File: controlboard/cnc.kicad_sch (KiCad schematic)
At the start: 31 parts, among them J1 Conn_02x04_Counter_Clockwise, J2 Conn_02x04_Row_Letter_Last, J5 Conn_02x04_Row_Letter_First, M1 Motor_Servo, Q1 PMOS AO3401A

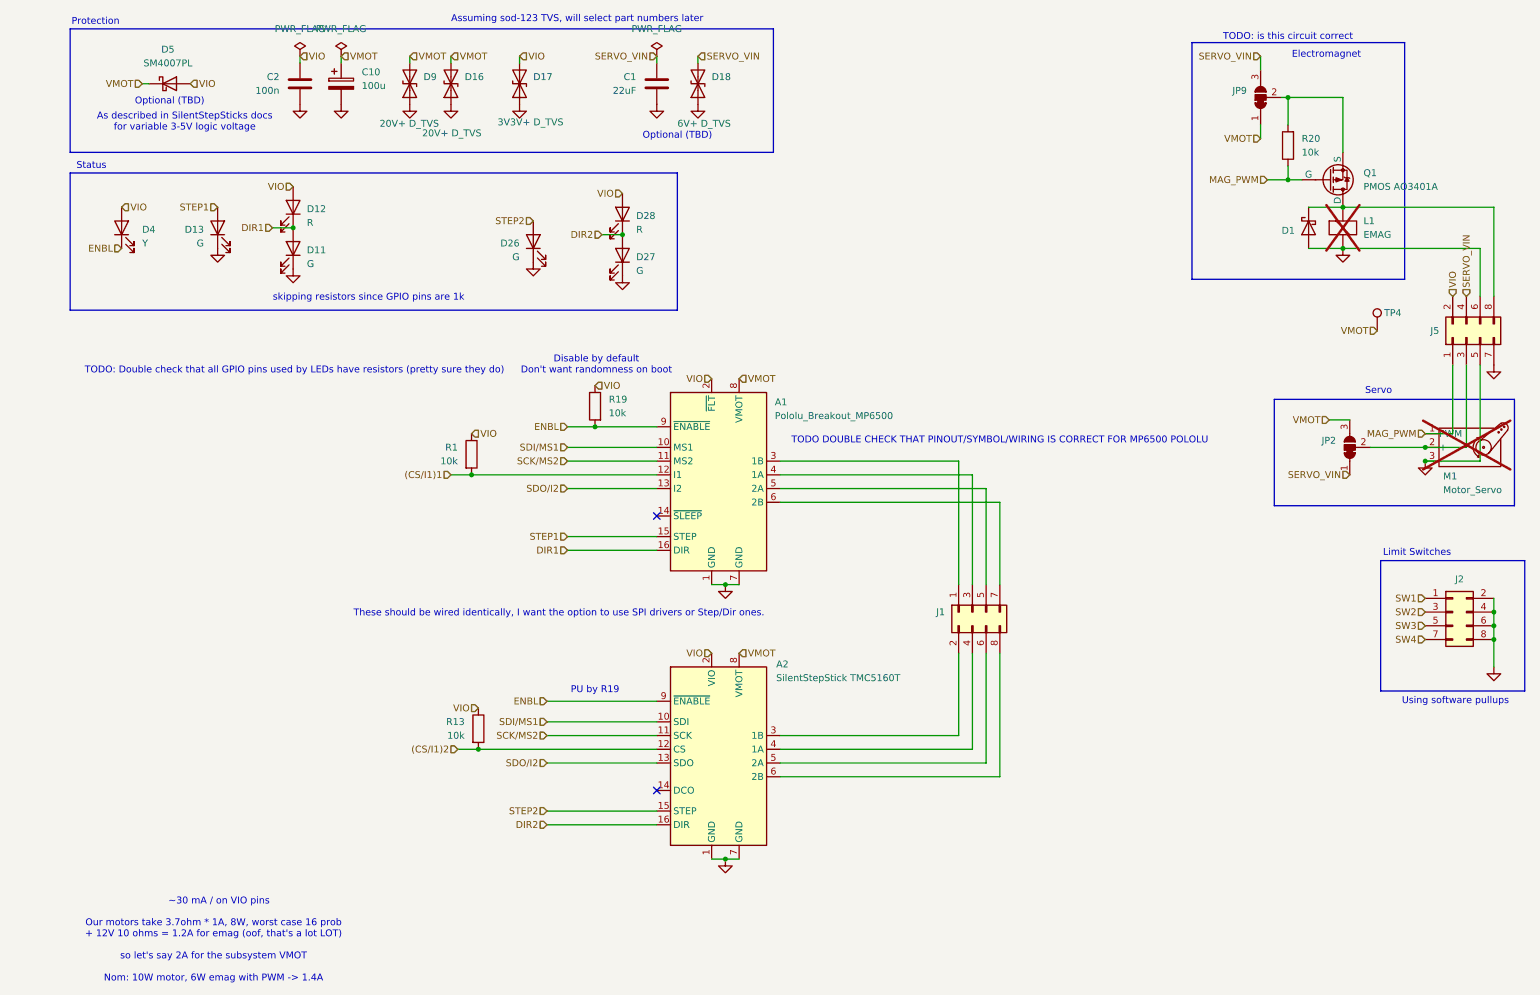
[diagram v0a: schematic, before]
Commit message: controlboard: fix critical mosfet errors
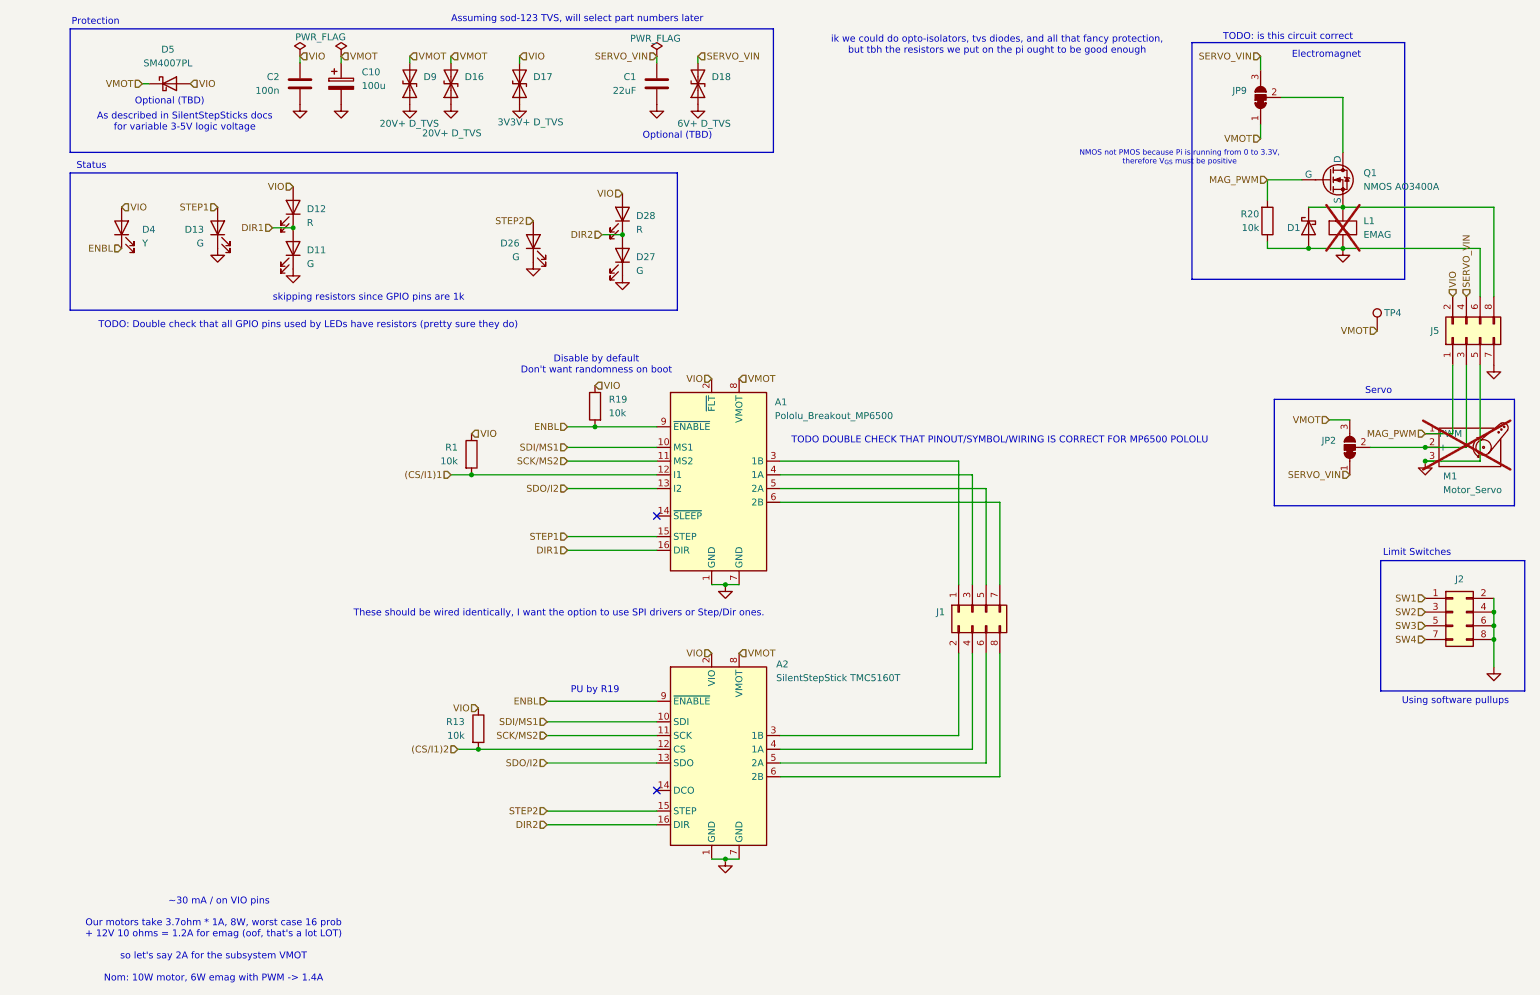
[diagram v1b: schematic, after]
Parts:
- removed Q1: PMOS AO3401A, Package_TO_SOT_SMD:SOT-23, symbol Simulation_SPICE:PMOS
- added Q1: NMOS AO3400A, Package_TO_SOT_SMD:SOT-23_Handsoldering, symbol Simulation_SPICE:NMOS
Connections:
- net GND: now also R20.1
- net MAG_PWM: now also R20.2, Q1.2 (G); no longer R20.1
- net at D1.1 (K), J5.8 (Pin_8), L1.1 (-): now also Q1.3 (S)
- net at JP9.2 (C): now also Q1.1 (D); no longer R20.2
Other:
- note added: "NMOS not PMOS because Pi is running from 0 to 3.3V, therefore V_{GS} must be positive"
- note added: "ik we could do opto-isolators, tvs diodes, and all that fancy protection, but tbh the resistors we put on the pi ought to be good enough"

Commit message: improvements
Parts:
- removed D16: 20V+ D_TVS, Diode_SMD:D_SOD-123F, symbol Device:D_TVS
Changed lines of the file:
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@@
 	(wire
 		(pts
-			(xy 83.82 22.86) (xy 83.82 24.13)
-		)
-		(stroke
-			(width 0)
-			(type default)
-		)
-	)
-	(wire
-		(pts
 			(xy 134.62 120.65) (xy 137.16 120.65)
 		)
@@
 		)
 	)
-	(hierarchical_label "VMOT"
-		(shape input)
-		(at 83.82 22.86 0)
-		(fields_autoplaced yes)
-		(effects
-			(font
-				(size 1.27 1.27)
-			)
-			(justify left)
-		)
-	)
 	(hierarchical_label "VIO"
 		(shape input)
@@
 	(symbol
 		(lib_id "Device:D_TVS")
-		(at 83.82 27.94 90)
-		(unit 1)
-		(exclude_from_sim no)
-		(in_bom yes)
-		(on_board yes)
-		(dnp no)
-		(property "Reference" "D16"
-			(at 86.36 26.6699 90)
-			(effects
-				(font
-					(size 1.27 1.27)
-				)
-				(justify right)
-			)
-		)
-		(property "Value" "20V+ D_TVS"
-			(at 78.486 37.084 90)
-			(effects
-				(font
-					(size 1.27 1.27)
-				)
-				(justify right)
-			)
-		)
-		(property "Footprint" "Diode_SMD:D_SOD-123F"
-			(at 83.82 27.94 0)
-			(effects
-				(font
-					(size 1.27 1.27)
-				)
-				(hide yes)
-			)
-		)
-		(property "Datasheet" "~"
-			(at 83.82 27.94 0)
-			(effects
-				(font
-					(size 1.27 1.27)
-				)
-				(hide yes)
-			)
-		)
-		(property "Description" "Bidirectional transient-voltage-suppression diode"
-			(at 83.82 27.94 0)
-			(effects
-				(font
-					(size 1.27 1.27)
-				)
-				(hide yes)
-			)
-		)
-		(pin "1"
-		)
-		(pin "2"
-		)
-		(instances
-			(project "controlboard"
-				(path "/2797250d-6fee-4769-b4dd-0e20ce4f0941/5be4ea58-2822-4c96-82fa-ac7323f92cc7"
-					(reference "D16")
-					(unit 1)
-				)
-			)
-		)
-	)
-	(symbol
-		(lib_id "Device:D_TVS")
 		(at 76.2 27.94 90)
 		(unit 1)
@@
 					(unit 1)
 				)
-			)
-		)
-	)
-	(symbol
-		(lib_id "power:GND")
-		(at 83.82 31.75 0)
-		(unit 1)
-		(exclude_from_sim no)
-		(in_bom yes)
-		(on_board yes)
-		(dnp no)
-		(fields_autoplaced yes)
-		(property "Reference" "#PWR010"
-			(at 83.82 38.1 0)
-			(effects
-				(font
-					(size 1.27 1.27)
-				)
-				(hide yes)
-			)
-		)
-		(property "Value" "GND"
-			(at 83.82 36.83 0)
-			(effects
-				(font
-					(size 1.27 1.27)
-				)
-				(hide yes)
-			)
-		)
-		(property "Footprint" ""
-			(at 83.82 31.75 0)
-			(effects
-				(font
-					(size 1.27 1.27)
-				)
-				(hide yes)
-			)
-		)
-		(property "Datasheet" ""
-			(at 83.82 31.75 0)
-			(effects
-				(font
-					(size 1.27 1.27)
-				)
-				(hide yes)
-			)
-		)
-		(property "Description" "Power symbol creates a global label with name \"GND\" , ground"
-			(at 83.82 31.75 0)
-			(effects
-				(font
-					(size 1.27 1.27)
-				)
-				(hide yes)
-			)
-		)
-		(pin "1"
-		)
-		(instances
-			(project "controlboard"
-				(path "/2797250d-6fee-4769-b4dd-0e20ce4f0941/5be4ea58-2822-4c96-82fa-ac7323f92cc7"
-					(reference "#PWR010")
-					(unit 1)
-				)

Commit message: controlboard finalized and ordered!!!
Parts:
- D17, D18, D9: LCSC (none) -> C123807
- Q1: LCSC (none) -> AO3400A

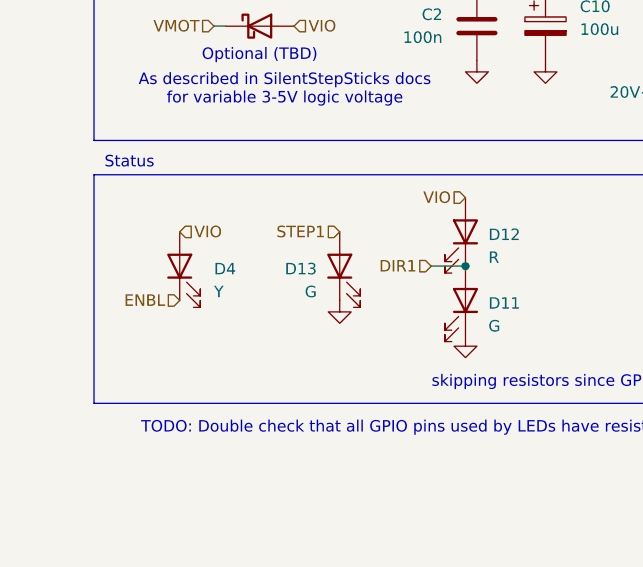
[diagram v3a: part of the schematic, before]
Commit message: Control board changes
Made a few control board changes (green checks on discord)
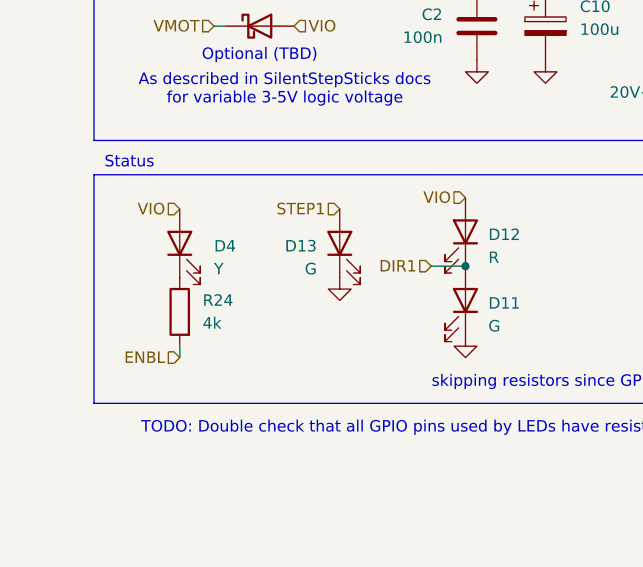
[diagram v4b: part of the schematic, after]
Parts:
- added R24: 4k, Resistor_SMD:R_0603_1608Metric_Pad0.98x0.95mm_HandSolder, symbol Device:R
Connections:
- net ENBL: now also R24.2; no longer D4.1 (K)
- new net: D4.1 (K), R24.1
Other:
- moved on the sheet: D13, D4
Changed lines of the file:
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@@
 	(wire
 		(pts
+			(xy 22.86 64.77) (xy 22.86 63.5)
+		)
+		(stroke
+			(width 0)
+			(type default)
+		)
+	)
+	(wire
+		(pts
 			(xy 234.95 57.15) (xy 234.95 58.42)
 		)
@@
 	(hierarchical_label "ENBL"
 		(shape input)
-		(at 22.86 58.42 180)
+		(at 22.86 64.77 180)
 		(fields_autoplaced yes)
 		(effects
@@
 	(hierarchical_label "STEP1"
 		(shape input)
-		(at 40.64 50.8 180)
+		(at 40.64 48.26 180)
 		(fields_autoplaced yes)
 		(effects
@@
 	(hierarchical_label "VIO"
 		(shape input)
-		(at 22.86 50.8 0)
+		(at 22.86 48.26 180)
 		(fields_autoplaced yes)
 		(effects
@@
 				(size 1.27 1.27)
 			)
-			(justify left)
+			(justify right)
 		)
 	)
@@
 	(symbol
 		(lib_id "power:GND")
-		(at 40.64 58.42 0)
+		(at 40.64 55.88 0)
 		(unit 1)
 		(exclude_from_sim no)
@@
 		(fields_autoplaced yes)
 		(property "Reference" "#PWR033"
-			(at 40.64 64.77 0)
+			(at 40.64 62.23 0)
 			(effects
 				(font
@@
 		)
 		(property "Value" "GND"
-			(at 40.64 63.5 0)
+			(at 40.64 60.96 0)
 			(effects
 				(font
@@
 		)
 		(property "Footprint" ""
-			(at 40.64 58.42 0)
+			(at 40.64 55.88 0)
 			(effects
 				(font
@@
 		)
 		(property "Datasheet" ""
-			(at 40.64 58.42 0)
+			(at 40.64 55.88 0)
 			(effects
 				(font
@@
 		)
 		(property "Description" "Power symbol creates a global label with name \"GND\" , ground"
-			(at 40.64 58.42 0)
+			(at 40.64 55.88 0)
 			(effects
 				(font
@@
 	(symbol
 		(lib_id "Device:LED")
-		(at 22.86 54.61 90)
+		(at 22.86 52.07 90)
 		(unit 1)
 		(exclude_from_sim no)
@@
 		(fields_autoplaced yes)
 		(property "Reference" "D4"
-			(at 26.67 54.9274 90)
+			(at 26.67 52.3874 90)
 			(effects
 				(font
@@
 		)
 		(property "Value" "Y"
-			(at 26.67 57.4674 90)
+			(at 26.67 54.9274 90)
 			(effects
 				(font
@@
 		)
 		(property "Footprint" "LED_SMD:LED_0603_1608Metric_Pad1.05x0.95mm_HandSolder"
-			(at 22.86 54.61 0)
+			(at 22.86 52.07 0)
 			(effects
 				(font
@@
 		)
 		(property "Datasheet" "~"
-			(at 22.86 54.61 0)
+			(at 22.86 52.07 0)
 			(effects
 				(font
@@
 		)
 		(property "Description" "Light emitting diode"
-			(at 22.86 54.61 0)
+			(at 22.86 52.07 0)
 			(effects
 				(font
@@
 		)
 		(property "JLCPCB Rotation Offset" ""
-			(at 22.86 54.61 0)
+			(at 22.86 52.07 0)
 			(effects
 				(font
@@
 	)
 	(symbol
+		(lib_id "Device:R")
+		(at 22.86 59.69 0)
+		(mirror y)
+		(unit 1)
+		(exclude_from_sim no)
+		(in_bom yes)
+		(on_board yes)
+		(dnp no)
+		(property "Reference" "R24"
+			(at 25.4 58.4199 0)
+			(effects
+				(font
+					(size 1.27 1.27)
+				)
+				(justify right)
+			)
+		)
+		(property "Value" "4k"
+			(at 25.4 60.9599 0)
+			(effects
+				(font
+					(size 1.27 1.27)
+				)
+				(justify right)
+			)
+		)
+		(property "Footprint" "Resistor_SMD:R_0603_1608Metric_Pad0.98x0.95mm_HandSolder"
+			(at 24.638 59.69 90)
+			(effects
+				(font
+					(size 1.27 1.27)
+				)
+				(hide yes)
+			)
+		)
+		(property "Datasheet" "~"
+			(at 22.86 59.69 0)
+			(effects
+				(font
+					(size 1.27 1.27)
+				)
+				(hide yes)
+			)
+		)
+		(property "Description" "Resistor"
+			(at 22.86 59.69 0)
+			(effects
+				(font
+					(size 1.27 1.27)
+				)
+				(hide yes)
+			)
+		)
+		(property "JLCPCB Rotation Offset" ""
+			(at 22.86 59.69 0)
+			(effects
+				(font
+					(size 1.27 1.27)
+				)
+				(hide yes)
+			)
+		)
+		(pin "2"
+		)
+		(pin "1"
+		)
+		(instances
+			(project "controlboard"
+				(path "/2797250d-6fee-4769-b4dd-0e20ce4f0941/5be4ea58-2822-4c96-82fa-ac7323f92cc7"
+					(reference "R24")
+					(unit 1)
+				)
+			)
+		)
+	)
+	(symbol
 		(lib_id "0chessbot-parts:Pololu_Breakout_MP6500")
 		(at 132.08 100.33 0)
@@
 	(symbol
 		(lib_id "Device:LED")
-		(at 40.64 54.61 90)
+		(at 40.64 52.07 90)
 		(unit 1)
 		(exclude_from_sim no)
@@
 		(dnp no)
 		(property "Reference" "D13"
-			(at 38.1 54.9274 90)
+			(at 38.1 52.3874 90)
 			(effects
 				(font
@@
 		)
 		(property "Value" "G"
-			(at 38.1 57.4674 90)
+			(at 38.1 54.9274 90)
 			(effects
 				(font
@@
 		)
 		(property "Footprint" "LED_SMD:LED_0603_1608Metric_Pad1.05x0.95mm_HandSolder"
-			(at 40.64 54.61 0)
+			(at 40.64 52.07 0)
 			(effects
 				(font
@@
 		)
 		(property "Datasheet" "~"
-			(at 40.64 54.61 0)
+			(at 40.64 52.07 0)
 			(effects
 				(font
@@
 		)
 		(property "Description" "Light emitting diode"
-			(at 40.64 54.61 0)
+			(at 40.64 52.07 0)
 			(effects
 				(font
@@
 		)
 		(property "JLCPCB Rotation Offset" ""
-			(at 40.64 54.61 0)
+			(at 40.64 52.07 0)
 			(effects
 				(font
